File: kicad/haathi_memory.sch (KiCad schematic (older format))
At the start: 28 parts

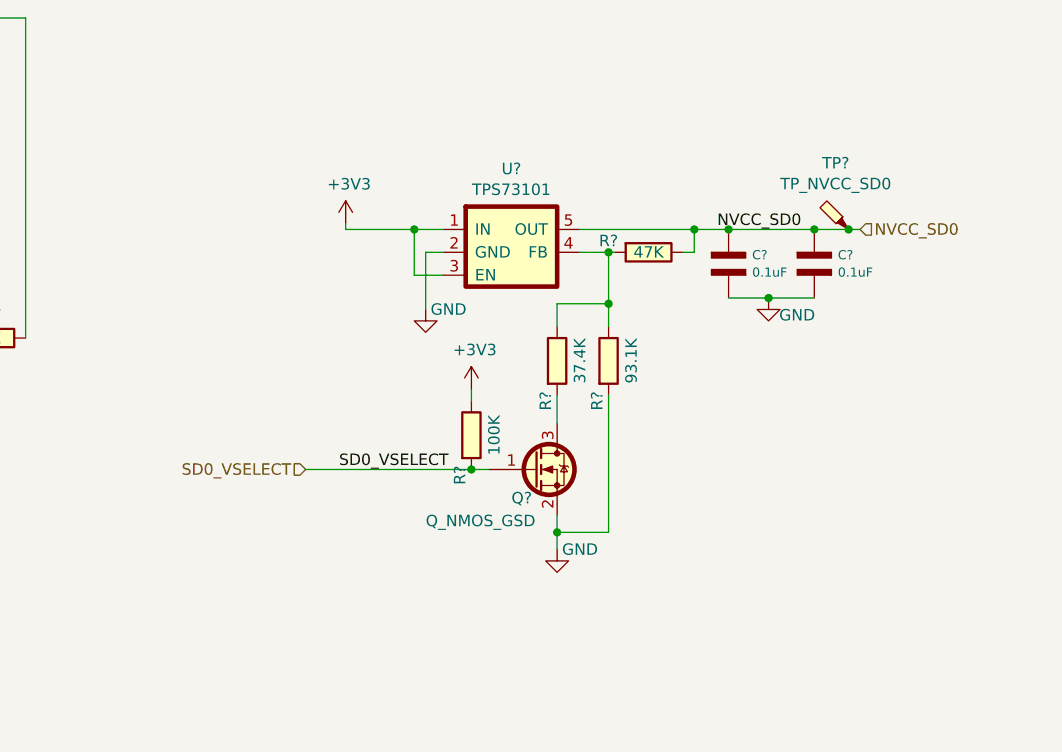
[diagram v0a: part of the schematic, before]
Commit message: Update SD Card voltage level select circuit
Signed-off-by: Kumar Abhishek <abhishek@theembeddedkitchen.net>
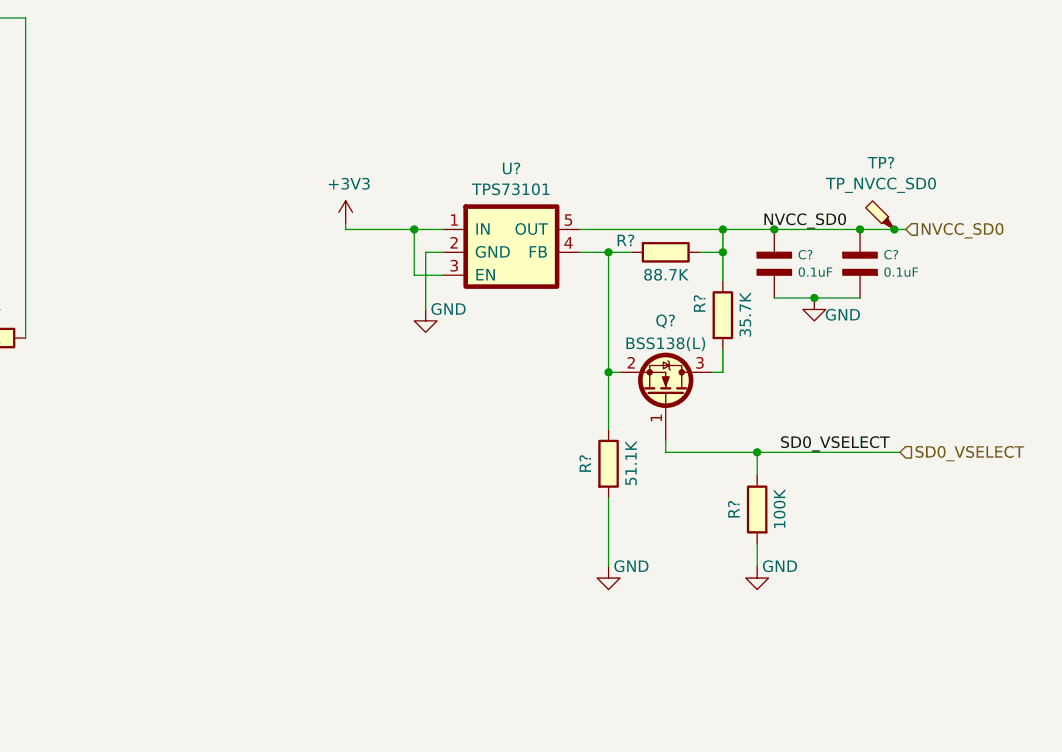
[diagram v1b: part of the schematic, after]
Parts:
- Q?: value Q_NMOS_GSD -> BSS138(L)
- R?: value 47K -> 88.7K
- R?: value 93.1K -> 51.1K
- R?: value 37.4K -> 35.7K
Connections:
- net +3V3: no longer R?.1
- net GND: now also R?.2; no longer Q?.2 (S)
- net NVCC_SD0: now also R?.1
- net SD0_VSELECT: now also R?.1; no longer R?.2
- net at R?.1, R?.2, U?.4 (FB): now also Q?.2 (S); no longer R?.1
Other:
- moved on the sheet: C?, Q?, R?, TP?
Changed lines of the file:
@@
 $Descr A4 11693 8268
 encoding utf-8
-Sheet 1 9
+Sheet 1 1
 Title "haathi_cam"
 Date "2018-03-11"
@@
 $EndComp
 Wire Wire Line
-	8925 2225 9425 2225
-Text HLabel 10150 2225 2    50   Input ~ 0
+	8925 2225 9550 2225
+Text HLabel 10350 2225 2    50   Input ~ 0
 NVCC_SD0
 $Comp
 L haathi_mayank:R R?
 U 1 1 5AA72443
-P 9225 2325
-F 0 "R?" V 9175 2150 50  0000 C CNN
-F 1 "47K" V 9225 2325 50  0000 C CNN
-F 2 "" V 9155 2325 30  0000 C CNN
-F 3 "" H 9225 2325 30  0000 C CNN
-	1    9225 2325
+P 9300 2325
+F 0 "R?" V 9250 2150 50  0000 C CNN
+F 1 "88.7K" V 9400 2325 50  0000 C CNN
+F 2 "" V 9230 2325 30  0000 C CNN
+F 3 "" H 9300 2325 30  0000 C CNN
+	1    9300 2325
 	0    1    1    0
 $EndComp
@@
 	8925 2325 9050 2325
 Wire Wire Line
-	9375 2325 9425 2325
-Wire Wire Line
-	9425 2325 9425 2225
-Connection ~ 9425 2225
+	9450 2325 9550 2325
+Wire Wire Line
+	9550 2325 9550 2225
 $Comp
 L haathi_mayank:R R?
 U 1 1 5AA771CB
-P 9050 2800
-F 0 "R?" V 9000 2625 50  0000 C CNN
-F 1 "93.1K" V 9150 2800 50  0000 C CNN
-F 2 "" V 8980 2800 30  0000 C CNN
-F 3 "" H 9050 2800 30  0000 C CNN
-	1    9050 2800
+P 9050 3250
+F 0 "R?" V 8950 3250 50  0000 C CNN
+F 1 "51.1K" V 9150 3250 50  0000 C CNN
+F 2 "" V 8980 3250 30  0000 C CNN
+F 3 "" H 9050 3250 30  0000 C CNN
+	1    9050 3250
 	1    0    0    -1
 $EndComp
 Connection ~ 9050 2325
 Wire Wire Line
-	9050 2325 9075 2325
+	9050 2325 9150 2325
 $Comp
 L haathi_mayank:C_NP C?
 U 1 1 5AA79ADE
-P 9575 2375
-F 0 "C?" H 9678 2413 40  0000 L CNN
-F 1 "0.1uF" H 9678 2337 40  0000 L CNN
-F 2 "" H 9575 2375 60  0000 C CNN
-F 3 "" H 9575 2375 60  0000 C CNN
-	1    9575 2375
+P 9775 2375
+F 0 "C?" H 9878 2413 40  0000 L CNN
+F 1 "0.1uF" H 9878 2337 40  0000 L CNN
+F 2 "" H 9775 2375 60  0000 C CNN
+F 3 "" H 9775 2375 60  0000 C CNN
+	1    9775 2375
 	1    0    0    -1
 $EndComp
@@
 L haathi_mayank:C_NP C?
 U 1 1 5AA79D25
-P 9950 2375
-F 0 "C?" H 10053 2413 40  0000 L CNN
-F 1 "0.1uF" H 10053 2337 40  0000 L CNN
-F 2 "" H 9950 2375 60  0000 C CNN
-F 3 "" H 9950 2375 60  0000 C CNN
-	1    9950 2375
-	1    0    0    -1
-$EndComp
-Wire Wire Line
-	9575 2525 9750 2525
+P 10150 2375
+F 0 "C?" H 10253 2413 40  0000 L CNN
+F 1 "0.1uF" H 10253 2337 40  0000 L CNN
+F 2 "" H 10150 2375 60  0000 C CNN
+F 3 "" H 10150 2375 60  0000 C CNN
+	1    10150 2375
+	1    0    0    -1
+$EndComp
+Wire Wire Line
+	9775 2525 9950 2525
 $Comp
 L power:GND #PWR?
 U 1 1 5AA7F108
-P 8825 3625
-F 0 "#PWR?" H 8825 3375 50  0001 C CNN
-F 1 "GND" H 8925 3625 50  0000 C CNN
-F 2 "" H 8825 3625 50  0001 C CNN
-F 3 "" H 8825 3625 50  0001 C CNN
-	1    8825 3625
+P 9050 3700
+F 0 "#PWR?" H 9050 3450 50  0001 C CNN
+F 1 "GND" H 9150 3700 50  0000 C CNN
+F 2 "" H 9050 3700 50  0001 C CNN
+F 3 "" H 9050 3700 50  0001 C CNN
+	1    9050 3700
 	1    0    0    -1
 $EndComp
@@
 L haathi_mayank:R R?
 U 1 1 5AA7F278
-P 8825 2800
-F 0 "R?" V 8775 2625 50  0000 C CNN
-F 1 "37.4K" V 8925 2800 50  0000 C CNN
-F 2 "" V 8755 2800 30  0000 C CNN
-F 3 "" H 8825 2800 30  0000 C CNN
-	1    8825 2800
-	1    0    0    -1
-$EndComp
-Wire Wire Line
-	9050 2325 9050 2550
+P 9550 2600
+F 0 "R?" V 9450 2650 50  0000 C CNN
+F 1 "35.7K" V 9650 2600 50  0000 C CNN
+F 2 "" V 9480 2600 30  0000 C CNN
+F 3 "" H 9550 2600 30  0000 C CNN
+	1    9550 2600
+	1    0    0    -1
+$EndComp
 $Comp
 L haathi_mayank:Q_NMOS_GSD Q?
 U 1 1 5AA85036
-P 8725 3275
-F 0 "Q?" H 8625 3150 50  0000 L CNN
-F 1 "Q_NMOS_GSD" H 8250 3050 50  0000 L CNN
-F 2 "" H 8925 3375 50  0001 C CNN
-F 3 "~" H 8725 3275 50  0001 C CNN
-	1    8725 3275
-	1    0    0    -1
-$EndComp
-Wire Wire Line
-	8825 3075 8825 2950
-Wire Wire Line
-	8825 2650 8825 2550
-Wire Wire Line
-	8825 2550 9050 2550
-Connection ~ 9050 2550
-Wire Wire Line
-	9050 2550 9050 2650
-Wire Wire Line
-	9425 2225 9575 2225
-Connection ~ 9575 2225
-Wire Wire Line
-	9575 2225 9950 2225
-Connection ~ 9950 2225
-Wire Wire Line
-	9950 2225 10100 2225
+P 9300 2950
+F 0 "Q?" V 9625 2950 50  0000 C CNN
+F 1 "BSS138(L)" V 9525 2950 50  0000 C CNN
+F 2 "" H 9500 3050 50  0001 C CNN
+F 3 "~" H 9300 2950 50  0001 C CNN
+	1    9300 2950
+	0    1    -1   0
+$EndComp
+Connection ~ 9775 2225
+Wire Wire Line
+	9775 2225 10150 2225
+Connection ~ 10150 2225
+Wire Wire Line
+	10150 2225 10300 2225
 $Comp
 L power:GND #PWR?
 U 1 1 5AA9887A
-P 9750 2525
-F 0 "#PWR?" H 9750 2275 50  0001 C CNN
-F 1 "GND" H 9875 2450 50  0000 C CNN
-F 2 "" H 9750 2525 50  0001 C CNN
-F 3 "" H 9750 2525 50  0001 C CNN
-	1    9750 2525
-	1    0    0    -1
-$EndComp
-Connection ~ 9750 2525
-Wire Wire Line
-	9750 2525 9950 2525
-Wire Wire Line
-	8825 3475 8825 3550
-Wire Wire Line
-	9050 2950 9050 3550
-Wire Wire Line
-	9050 3550 8825 3550
-Connection ~ 8825 3550
-Wire Wire Line
-	8825 3550 8825 3625
+P 9950 2525
+F 0 "#PWR?" H 9950 2275 50  0001 C CNN
+F 1 "GND" H 10075 2450 50  0000 C CNN
+F 2 "" H 9950 2525 50  0001 C CNN
+F 3 "" H 9950 2525 50  0001 C CNN
+	1    9950 2525
+	1    0    0    -1
+$EndComp
+Connection ~ 9950 2525
+Wire Wire Line
+	9950 2525 10150 2525
 $Comp
 L haathi_mayank:R R?
 U 1 1 5AA9E7B3
-P 8450 3125
-F 0 "R?" V 8400 2950 50  0000 C CNN
-F 1 "100K" V 8550 3125 50  0000 C CNN
-F 2 "" V 8380 3125 30  0000 C CNN
-F 3 "" H 8450 3125 30  0000 C CNN
-	1    8450 3125
-	1    0    0    -1
-$EndComp
-Wire Wire Line
-	8525 3275 8450 3275
-Connection ~ 8450 3275
-$Comp
-L power:+3V3 #PWR?
-U 1 1 5AAA1A38
-P 8450 2925
-F 0 "#PWR?" H 8450 2775 50  0001 C CNN
-F 1 "+3V3" H 8465 3098 50  0000 C CNN
-F 2 "" H 8450 2925 50  0001 C CNN
-F 3 "" H 8450 2925 50  0001 C CNN
-	1    8450 2925
-	1    0    0    -1
-$EndComp
-Wire Wire Line
-	8450 2925 8450 2975
-Text HLabel 7725 3275 0    50   Input ~ 0
+P 9700 3450
+F 0 "R?" V 9800 3450 50  0000 C CNN
+F 1 "100K" V 9600 3450 50  0000 C CNN
+F 2 "" V 9630 3450 30  0000 C CNN
+F 3 "" H 9700 3450 30  0000 C CNN
+	1    9700 3450
+	-1   0    0    -1
+$EndComp
+Text HLabel 10325 3200 2    50   Input ~ 0
 SD0_VSELECT
-Text Label 8350 3275 2    50   ~ 0
+Text Label 9800 3200 0    50   ~ 0
 SD0_VSELECT
-Wire Wire Line
-	7725 3275 8450 3275
 $Comp
 L haathi_mayank:Test_Point_Probe TP?
 U 1 1 5AAA9481
-P 10100 2225
-F 0 "TP?" V 10390 2281 50  0000 C CNN
-F 1 "TP_NVCC_SD0" V 10299 2281 50  0000 C CNN
-F 2 "" H 10300 2225 50  0001 C CNN
-F 3 "" H 10300 2225 50  0001 C CNN
-	1    10100 2225
+P 10300 2225
+F 0 "TP?" V 10590 2281 50  0000 C CNN
+F 1 "TP_NVCC_SD0" V 10499 2281 50  0000 C CNN
+F 2 "" H 10500 2225 50  0001 C CNN
+F 3 "" H 10500 2225 50  0001 C CNN
+	1    10300 2225
 	0    -1   -1   0
 $EndComp
-Connection ~ 10100 2225
-Wire Wire Line
-	10100 2225 10150 2225
-Text Label 9525 2225 0    50   ~ 0
+Connection ~ 10300 2225
+Wire Wire Line
+	10300 2225 10350 2225
+Text Label 9725 2225 0    50   ~ 0
 NVCC_SD0
 $Comp
@@
 Wire Wire Line
 	7775 5200 7825 5200
+Wire Wire Line
+	9550 2225 9775 2225
+Connection ~ 9550 2225
+Connection ~ 9550 2325
+Wire Wire Line
+	9550 2325 9550 2450
+Wire Wire Line
+	9050 2325 9050 2850
+Wire Wire Line
+	9550 2750 9550 2850
+Wire Wire Line
+	9100 2850 9050 2850
+Connection ~ 9050 2850
+Wire Wire Line
+	9050 2850 9050 3100
+Wire Wire Line
+	9500 2850 9550 2850
+Wire Wire Line
+	9050 3400 9050 3700
+Wire Wire Line
+	9300 3200 9300 3150
+Connection ~ 9700 3200
+Wire Wire Line
+	9700 3200 9300 3200
+Wire Wire Line
+	9700 3200 10325 3200
+Wire Wire Line
+	9700 3200 9700 3300
+Wire Wire Line
+	9700 3600 9700 3700
+$Comp
+L power:GND #PWR?
+U 1 1 5AC5D106
+P 9700 3700
+F 0 "#PWR?" H 9700 3450 50  0001 C CNN
+F 1 "GND" H 9800 3700 50  0000 C CNN
+F 2 "" H 9700 3700 50  0001 C CNN
+F 3 "" H 9700 3700 50  0001 C CNN
+	1    9700 3700
+	1    0    0    -1
+$EndComp
 $EndSCHEMATC

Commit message: Add the SD card power control MOS switch circuitry
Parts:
- added C?: 0.22u, symbol haathi_mayank:C_NP
- added C?: 0.1u, symbol haathi_mayank:C_NP
- added C?: 1u, symbol haathi_mayank:C_NP
- added D? (x2): D_Schottky, symbol haathi_mayank:D_Schottky
- added Q?: Q_PMOS_GDS, symbol haathi_mayank:Q_PMOS_GDS
- added Q? (x2): Q_NMOS_GSD, symbol haathi_mayank:Q_NMOS_GSD
- added R?: 22k, symbol haathi_mayank:R
- added R? (x2): 10k, symbol haathi_mayank:R
- added R?: 0E_DNP, symbol haathi_mayank:R
- added R?: 51, symbol haathi_mayank:R
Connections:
- net +3V3: now also C?.1 (+), Q?.3 (S), R?.1, R?.1, R?.2; no longer C6.1 (+), C7.1 (+), C8.1 (+), R8.1, SD1.4 (VCC)
- net GND: now also C?.2 (-), C?.2 (-), Q?.2 (S), Q?.2 (S)
- new net: C?.2 (-), Q?.1 (G), R?.1, R?.2
- new net: Q?.1 (G), Q?.3 (D), R?.2
- new net: C?.1 (+), D?.2 (A), D?.2 (A), Q?.1 (G), R?.2
- new net: Q?.3 (D), R?.2
- new net MCU_RESET_N: D?.1 (K)
- new net SD_PWREN: D?.1 (K)
- new net SD_VCC_3V3: C6.1 (+), C7.1 (+), C8.1 (+), C?.1 (+), Q?.2 (D), R8.1, R?.1, R?.1, SD1.4 (VCC)
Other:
- moved on the sheet: C?, R?, TP?, U?

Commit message: NVCC_SD0 and NVCC_SD1 are generated in this sheet now
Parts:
- added R? (x2): 10k, symbol haathi:R
- added R?: 0E_DNP, symbol haathi_mayank:R
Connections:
- net +1V8: now also R?.1
- net NVCC_SD0: now also R?.1, R?.1
- net SD1_CMD: now also R?.2
- net SD1_D0: now also R?.2
- new net NVCC_SD1: R?.2
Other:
- moved on the sheet: C?, Q?, R?, TP?, U?

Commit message: Annotated schematic
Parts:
- gave numbers to parts that had none: 34

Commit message: ERC pass 1: Check and resolve the errors
Signed-off-by: Kumar Abhishek <abhishek@theembeddedkitchen.net>
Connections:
- wire segments 174 -> 175
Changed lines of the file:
@@
 EESchema Schematic File Version 4
-LIBS:haathi_schematic-cache
+LIBS:haathi-cache
 EELAYER 26 0
 EELAYER END
 $Descr A4 11693 8268
 encoding utf-8
-Sheet 4 9
+Sheet 4 11
 Title "haathi_cam"
 Date "2018-03-11"
@@
 Text HLabel 1875 4625 0    50   Input ~ 0
 NVCC_SD1
+$Comp
+L power:PWR_FLAG #FLG0102
+U 1 1 5B26A5D8
+P 6900 5100
+F 0 "#FLG0102" H 6900 5175 50  0001 C CNN
+F 1 "PWR_FLAG" H 6900 5274 50  0000 C CNN
+F 2 "" H 6900 5100 50  0001 C CNN
+F 3 "~" H 6900 5100 50  0001 C CNN
+	1    6900 5100
+	1    0    0    -1
+$EndComp
+Wire Wire Line
+	6900 5100 6575 5100
+Connection ~ 6575 5100
 $EndSCHEMATC
